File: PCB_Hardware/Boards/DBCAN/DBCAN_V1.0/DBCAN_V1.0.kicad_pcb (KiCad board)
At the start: 4 copper layers, 47 x 30 mm, 55 parts, among them J1 Conn_ARM_SWD_TagConnect_TC203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, J11 GT-USB-7010ASV, J2 SM04B-PASS-TBT, J3 SM04B-PASS-TBT, Q1 SI2302, Q2 SI2302, Q3 SI2302, Q4 SI2302, U1 STM32G0B1KBT6TR, U10 TPD2E2U06DCK, U16 CAT24C256, U2 TCAN1048AVDMTRQ1, U3 MCP1802T-3302I/OT, Y1 ASEMB-8.000MHZ-XY-T

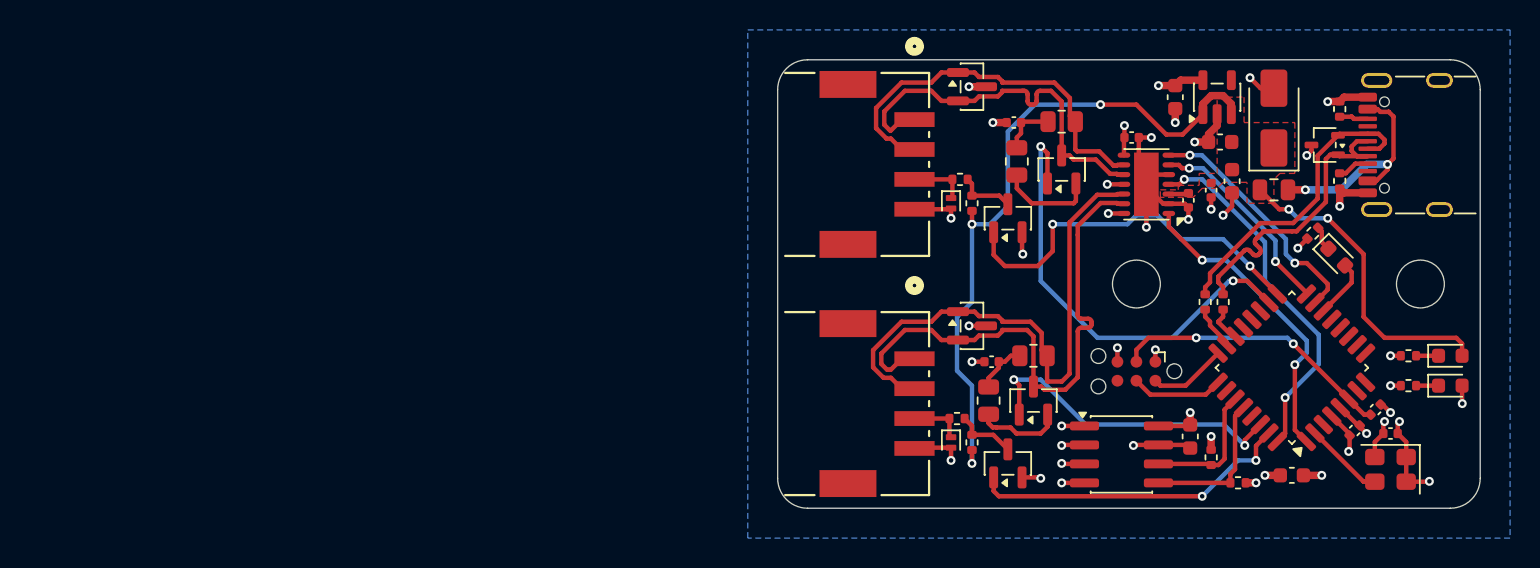
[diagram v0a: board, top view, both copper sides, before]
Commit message: Completed board layout and tweaks to schematic. Added 3D model lib
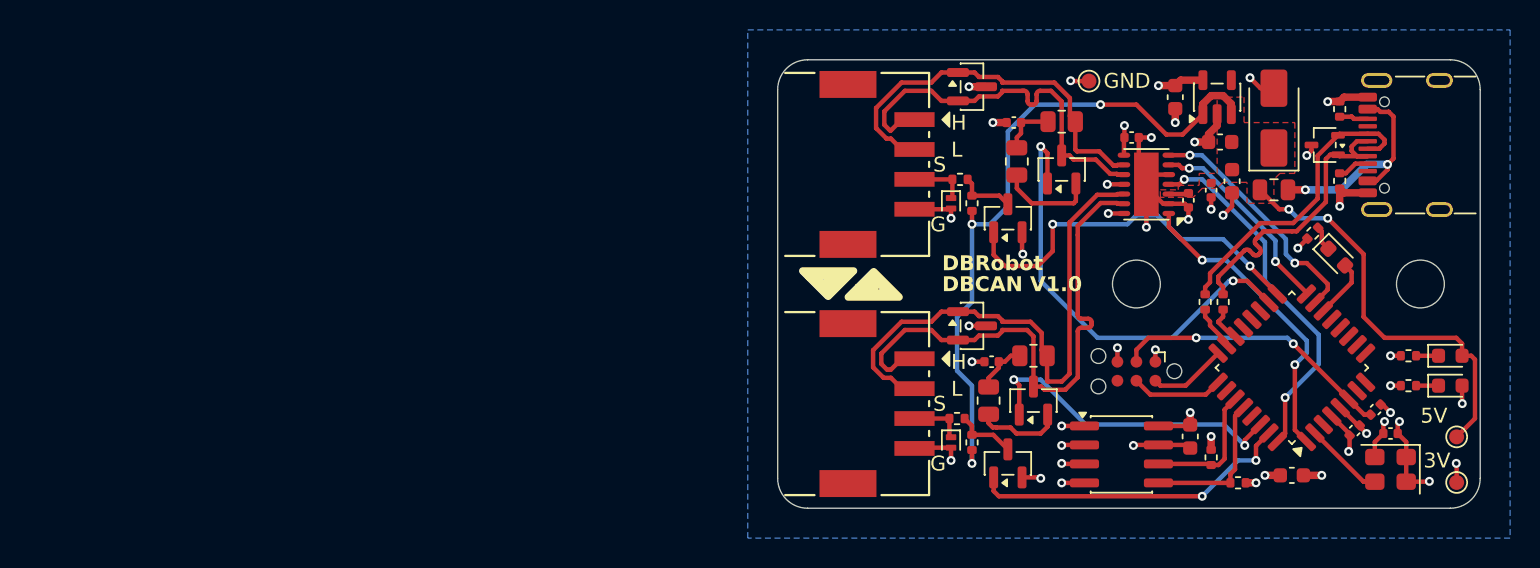
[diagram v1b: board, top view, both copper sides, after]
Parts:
- added TP1: TestPoint, TestPoint:TestPoint_Pad_D1.0mm, F.Cu at (185.4, 98.2)
- added TP2: TestPoint, TestPoint:TestPoint_Pad_D1.0mm, F.Cu at (185.4, 101.3)
- added TP3: TestPoint, TestPoint:TestPoint_Pad_D1.0mm, F.Cu at (160.8, 74.4)
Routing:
- net +5V: track 67.8 -> 74.5 mm
- net +3.3V: track 23.6 -> 24.9 mm, vias 13 -> 14
- net GND: track 62.1 -> 63.4 mm, vias 32 -> 33
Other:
- board text added: "1"
- board text added: "2"
- board text added: "3V"
- board text added: "5V"
- board text added: "DBCAN V1.0"
- board text added: "DBRobot"
- board text added: "G"
- board text added: "GND"
- board text added: "H"
- board text added: "L"
- board text added: "S"

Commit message: First version of DBCAN board
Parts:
- removed C37: 4.7u, Capacitor_SMD:C_0603_1608Metric
- removed C38, C6, C7: 100n, Capacitor_SMD:C_0402_1005Metric
- removed C39, C40: 1u, Capacitor_SMD:C_0603_1608Metric
- removed C46: 100n, Capacitor_SMD:C_0603_1608Metric
- removed C8: 10n, Capacitor_SMD:C_0402_1005Metric
- removed D10: SMAJ5.0A, Diode_SMD:D_SMA
- removed J11: GT-USB-7010ASV, Connector_USB:USB_C_Receptacle_G-Switch_GT-USB-7010ASV
- removed R1, R2: 60, Resistor_SMD:R_0805_2012Metric
- removed R27, R28: 4.7k, Resistor_SMD:R_0402_1005Metric
- removed R47, R48: 5.1k, Resistor_SMD:R_0402_1005Metric
- removed R49, R50, R53: 2.2k, Resistor_SMD:R_0402_1005Metric
- removed R51, R52: 22, Resistor_SMD:R_0402_1005Metric
- removed U10: TPD2E2U06DCK, Package_TO_SOT_SMD:SOT-323_SC-70
- removed U16: CAT24C256, Package_SO:SOIC-8_3.9x4.9mm_P1.27mm
- added C11: 4.7u, Capacitor_SMD:C_0603_1608Metric, F.Cu at (131.6, 79.8)
- added C12: 100n, Capacitor_SMD:C_0402_1005Metric, F.Cu at (131.0, 78.4)
- added C13: 1u, Capacitor_SMD:C_0603_1608Metric, F.Cu at (127.6, 77.2)
- added C14: 1u, Capacitor_SMD:C_0603_1608Metric, F.Cu at (124.2, 79.8)
- added C15: 100n, Capacitor_SMD:C_0402_1005Metric, F.Cu at (119.2, 88.6)
- added C16: 100n, Capacitor_SMD:C_0402_1005Metric, F.Cu at (115.2, 90.8)
- added C17: 4.7n, Capacitor_SMD:C_0402_1005Metric, F.Cu at (103.8, 91.7)
- added C18: 4.7n, Capacitor_SMD:C_0402_1005Metric, F.Cu at (117.4, 78.4)
- added D8: BLUE, LED_SMD:LED_0603_1608Metric, F.Cu at (126.6, 90.0)
- added J4: SM04B-PASS-TBT, DBRobot:CONN_JST_SM04B-PASS, F.Cu at (95.0, 83.0)
- added R10: 60.4, Resistor_SMD:R_0805_2012Metric, F.Cu at (104.2, 88.9)
- added R11: 60.4, Resistor_SMD:R_0805_2012Metric, F.Cu at (115.8, 81.2)
- added R12: 60.4, Resistor_SMD:R_0805_2012Metric, F.Cu at (115.0, 78.4)
- added R13: 10k, Resistor_SMD:R_0402_1005Metric, F.Cu at (113.0, 92.4)
- added R14: 10k, Resistor_SMD:R_0402_1005Metric, F.Cu at (115.6, 93.8)
- added R15: 1k, Resistor_SMD:R_0402_1005Metric, F.Cu at (103.3, 97.4)
- added R16: 1k, Resistor_SMD:R_0402_1005Metric, F.Cu at (102.4, 82.6)
- added R17: 2.2k, Resistor_SMD:R_0402_1005Metric, F.Cu at (123.8, 90.0)
- added R18: 0, Resistor_SMD:R_0402_1005Metric, F.Cu at (115.8, 100.4)
- added R9: 60.4, Resistor_SMD:R_0805_2012Metric, F.Cu at (107.0, 91.7)
- added TP10: TestPoint, TestPoint:TestPoint_Pad_D1.0mm, B.Cu at (92.0, 83.0)
- added TP11: TestPoint, TestPoint:TestPoint_Pad_D1.0mm, B.Cu at (102.0, 80.0)
- added TP12: TestPoint, TestPoint:TestPoint_Pad_D1.0mm, B.Cu at (136.0, 91.2)
- added TP13: TestPoint, TestPoint:TestPoint_Pad_D1.0mm, B.Cu at (136.0, 88.0)
- added TP14: TestPoint, TestPoint:TestPoint_Pad_D1.0mm, B.Cu at (129.0, 102.0)
- added TP4: TestPoint, TestPoint:TestPoint_Pad_D1.0mm, B.Cu at (126.0, 100.0)
- added TP5: TestPoint, TestPoint:TestPoint_Pad_D1.0mm, B.Cu at (129.0, 97.0)
- added TP6: TestPoint, TestPoint:TestPoint_Pad_D1.0mm, B.Cu at (92.0, 94.0)
- added TP7: TestPoint, TestPoint:TestPoint_Pad_D1.0mm, B.Cu at (92.0, 97.0)
- added TP8: TestPoint, TestPoint:TestPoint_Pad_D1.0mm, B.Cu at (92.0, 100.0)
- added TP9: TestPoint, TestPoint:TestPoint_Pad_D1.0mm, B.Cu at (92.0, 80.0)
- added U4: TCAN1048AVDMTRQ1, Package_DFN_QFN:DFN-14-1EP_3x4.5mm_P0.65mm_EP1.65x4.25mm, F.Cu at (116.2, 87.5)
- C4, C5: value 4.7n -> 100n
- D2: value PESD1CAN -> SMAJ5.0A; footprint Package_TO_SOT_SMD:SOT-23 -> Diode_SMD:D_SMA
- D3: value PESD1CAN -> RED; footprint Package_TO_SOT_SMD:SOT-23 -> LED_SMD:LED_0603_1608Metric
- D4: value RED -> PESD5V0L1UL; footprint LED_SMD:LED_0603_1608Metric -> Diode_SMD:D_SOD-882
- D5, D6: value PESD5V0L1UL -> PESD1CAN; footprint Diode_SMD:D_SOD-882 -> Package_TO_SOT_SMD:SOT-23
- D7: value BLUE -> PESD5V0L1UL; footprint LED_SMD:LED_0603_1608Metric -> Diode_SMD:D_SOD-882
- F1: value MF-PSMF050X-2 -> BSMD0805-050-24V
- J1: value Conn_ARM_SWD_TagConnect_TC2030-NL -> Conn_ARM_SWD_TagConnect_TC2030; footprint Connector:Tag-Connect_TC2030-IDC-NL_2x03_P1.27mm_Vertical -> Connector:Tag-Connect_TC2030-IDC-FP_2x03_P1.27mm_Vertical
- J2: value SM04B-PASS-TBT -> GT-USB-7010ASV; footprint DBRobot:CONN_JST_SM04B-PASS -> Connector_USB:USB_C_Receptacle_G-Switch_GT-USB-7010ASV
- R3, R4: value 60 -> 2.2k; footprint Resistor_SMD:R_0805_2012Metric -> Resistor_SMD:R_0402_1005Metric
- R5, R6: value 10k -> 5.1k
- R7, R8: value 100k -> 0
- TP1, TP2, TP3: moved to B.Cu
- U1: value STM32G0B1KBT6TR -> STM32G0B1KBT6
- U2: value TCAN1048AVDMTRQ1 -> MCP1802T-3302I/OT; footprint Package_DFN_QFN:DFN-14-1EP_3x4.5mm_P0.65mm_EP1.65x4.25mm -> Package_TO_SOT_SMD:SOT-23-5
- U3: value MCP1802T-3302I/OT -> TPD2E2U06DCK; footprint Package_TO_SOT_SMD:SOT-23-5 -> Package_TO_SOT_SMD:SOT-323_SC-70
- Y1: value ASEMB-8.000MHZ-XY-T -> ASEM1-24.000MHZ-LC-T
- moved D4 83.5 mm to (101.6, 98.5), turned to -90 degrees
- moved H2 76.4 mm to (107.0, 80.0)
- moved D7 75.6 mm to (101.8, 84.4), turned to -90 degrees
- moved Y1 68.2 mm to (112.8, 101.4), turned to -90 degrees
- moved TP1 64.3 mm to (123.0, 83.0), turned to 180 degrees
- moved C3 60.6 mm to (110.4, 102.8)
- moved C2 60.5 mm to (118.2, 101.4), turned to -45 degrees
- moved TP2 60.3 mm to (128.0, 83.0), turned to 180 degrees
- moved H1 58.2 mm to (107.0, 100.0)
- moved C1 57.4 mm to (117.0, 102.2), turned to -45 degrees
- moved J3 52.8 mm to (95.0, 97.0)
- moved U1 52.1 mm to (122.4, 97.2), turned to 45 degrees
- moved Q1 50.6 mm to (107.0, 88.7), turned to -90 degrees
- moved D5 50.3 mm to (102.9, 95.0), turned to 180 degrees
- moved D1 48.8 mm to (138.4, 78.4), turned to 180 degrees
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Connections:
- C3 pad 1: +5V -> +3.3V
- C4 pad 1: Net-(C4-Pad1) -> +3.3V
- C5 pad 1: Net-(C5-Pad1) -> GND
- C5 pad 2: GND -> /MCU/NRST
- D1 pad 2: +5V -> +3.3V
- D2 pad 1: /CANFD/CANFD1- -> +5V
- D2 pad 2: /CANFD/CANFD1+ -> GND
- D3 pad 1: /CANFD/CANFD2- -> Net-(D3-K)
- D3 pad 2: /CANFD/CANFD2+ -> +5V
- D4 pad 1: Net-(D4-K) -> /CANFD/SEQ1_PIN
- D4 pad 2: +3.3V -> GND
- D5 pad 1: Net-(D5-K) -> /CANFD/CANFD1-
- D5 pad 2: GND -> /CANFD/CANFD1+
- D6 pad 1: Net-(D6-K) -> /CANFD/CANFD2-
- D6 pad 2: GND -> /CANFD/CANFD2+
- D7 pad 1: Net-(D7-K) -> /CANFD/SEQ2_PIN
- D7 pad 2: Net-(D7-A) -> GND
- J3 pad 1: /CANFD/CANFD2+ -> /CANFD/CANFD1+
- J3 pad 2: /CANFD/CANFD2- -> /CANFD/CANFD1-
- J3 pad 3: Net-(D5-K) -> /CANFD/SEQ1_PIN
- R3 pad 1: /CANFD/CANFD2- -> GND
- R3 pad 2: Net-(C5-Pad1) -> Net-(D1-K)
- R4 pad 1: Net-(C5-Pad1) -> GND
- R4 pad 2: Net-(Q2-S) -> Net-(D3-K)
- R5 pad 1: Net-(Q3-D) -> Net-(J2-CC1)
- R5 pad 2: +5V -> GND
- R6 pad 1: Net-(Q4-D) -> Net-(J2-CC2)
- R6 pad 2: +5V -> GND
- R7 pad 1: Net-(D6-K) -> /MCU/USB_D-
- R7 pad 2: Net-(Q3-D) -> /USB/D-
- R8 pad 1: Net-(D5-K) -> /MCU/USB_D+
- R8 pad 2: Net-(Q4-D) -> /USB/D+
- TP1 pad 1: +5V -> +3.3V
- TP2 pad 1: +3.3V -> +5V
- U1 pad 1: /CANFD/CANFD_TX1 -> /CANFD/CANFD_TX2
- U1 pad 14: Net-(D7-A) -> unconnected-(U1-PA7-Pad14)
- U1 pad 15: /CANFD/CANFD_RX2 -> unconnected-(U1-PB0-Pad15)
- U1 pad 16: /CANFD/CANFD_TX2 -> unconnected-(U1-PB1-Pad16)
- U1 pad 17: /CANFD/SEQ2 -> unconnected-(U1-PB2-Pad17)
- U1 pad 18: /CANFD/TERM_R2 -> Net-(D8-A)
- U1 pad 26: unconnected-(U1-PA15-Pad26) -> /CANFD/TERM_R2
- U1 pad 27: /EEPROM/EEPROM_SCL -> unconnected-(U1-PB3-Pad27)
- U1 pad 28: /EEPROM/EEPROM_SDA -> unconnected-(U1-PB4-Pad28)
- U1 pad 29: unconnected-(U1-PB5-Pad29) -> /CANFD/CANFD_RX1
- U1 pad 3: unconnected-(U1-PC15-Pad3) -> /CANFD/SEQ1
- U1 pad 30: /CANFD/TERM_R1 -> /CANFD/CANFD_TX1
- U1 pad 31: /CANFD/SEQ1 -> /CANFD/TERM_R1
- U1 pad 32: /CANFD/CANFD_RX1 -> /CANFD/CANFD_RX2
- U1 pad 7: unconnected-(U1-PA0-Pad7) -> /CANFD/SEQ2
- U2 pad 1: /CANFD/CANFD_TX1 -> +5V
- U2 pad 4: /CANFD/CANFD_RX1 -> unconnected-(U2-NC-Pad4)
- U2 pad 5: GND -> +3.3V
- U3 pad 1: +5V -> /USB/D-
- U3 pad 2: GND -> /USB/D+
- U3 pad 3: +5V -> GND
- Y1 pad 3: Net-(U1-PC14) -> Net-(Y1-OUT)
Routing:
- net /CANFD/CANFD2-: track 26.5 -> 79.1 mm, vias 0 -> 3
- net /CANFD/CANFD2+: track 26.4 -> 77.7 mm, vias 0 -> 3
- net Net-(Q4-D): track 3.85 -> 28.0 mm, vias 0 -> 4
- net +5V: track 74.5 -> 54.0 mm
- net /MCU/SWDIO: track 5.23 -> 21.7 mm, vias 0 -> 2
- net /CANFD/CANFD_TX1: track 20.7 -> 5.98 mm, vias 2 -> 0
- net /MCU/SWCLK: track 6.20 -> 19.3 mm, vias 0 -> 2
- net /CANFD/SEQ1_PIN: track 0.00 -> 12.0 mm, vias 0 -> 1
- net /CANFD/CANFD_RX1: track 24.3 -> 12.6 mm, vias 2 -> 0
- net /EEPROM/EEPROM_SDA: track 10.2 -> 0.00 mm
- net GND: track 63.4 -> 53.3 mm, vias 33 -> 30
- net /EEPROM/EEPROM_SCL: track 8.91 -> 0.00 mm
- net /CANFD/TERM_R2: track 30.7 -> 22.3 mm
- net /CANFD/SEQ2: track 25.5 -> 17.2 mm
- net /USB/D+: track 20.4 -> 12.3 mm, vias 0 -> 1
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- removed copper zone on F.Cu, net +5V
- removed copper zone on B.Cu, net GND
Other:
- board size 47 x 30 mm -> 50 x 28 mm
- board text added: "3.3V"
- board text added: "H1"
- board text added: "H2"
- board text added: "L1"
- board text added: "L2"
- board text added: "NRST"
- board text added: "SEQ1"
- board text added: "SEQ2"
- board text added: "SWCLK"
- board text added: "SWDIO"
- board text removed: "3V"
- board text removed: "S"
